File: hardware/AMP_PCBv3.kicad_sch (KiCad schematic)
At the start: 34 parts, among them CN10 Male_R2, CN7 Male_L1, J1 Input_PWR, U1 TPS56624x, U2 RFM95W-915S2

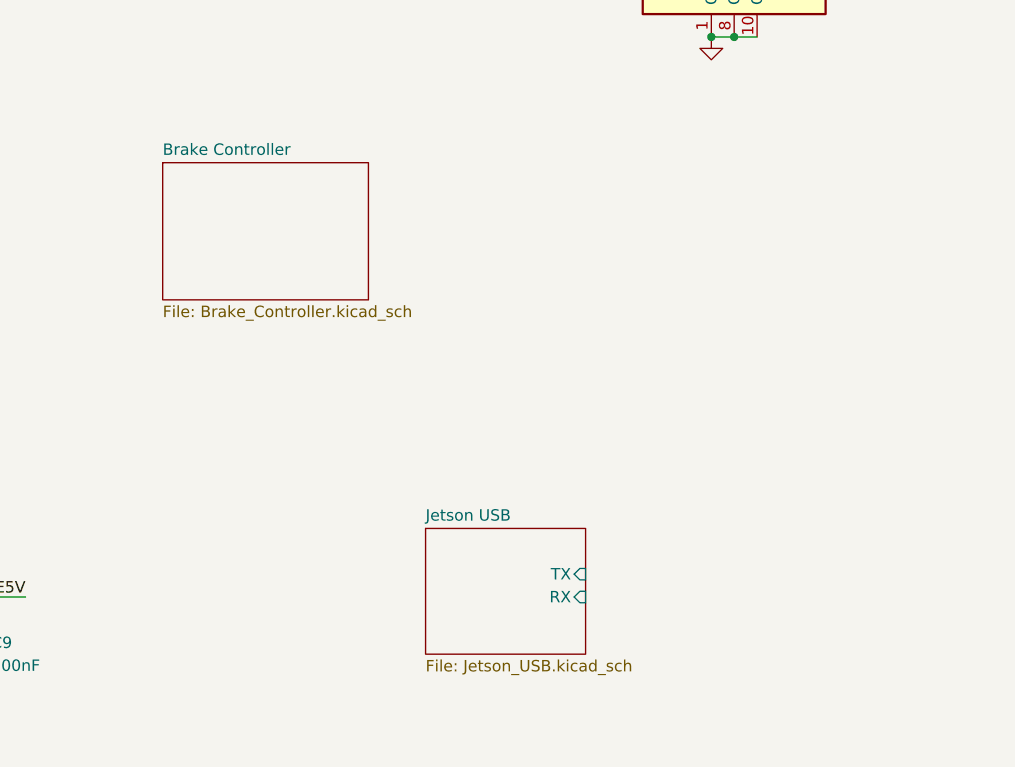
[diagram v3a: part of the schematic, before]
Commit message: Add IMU schematic
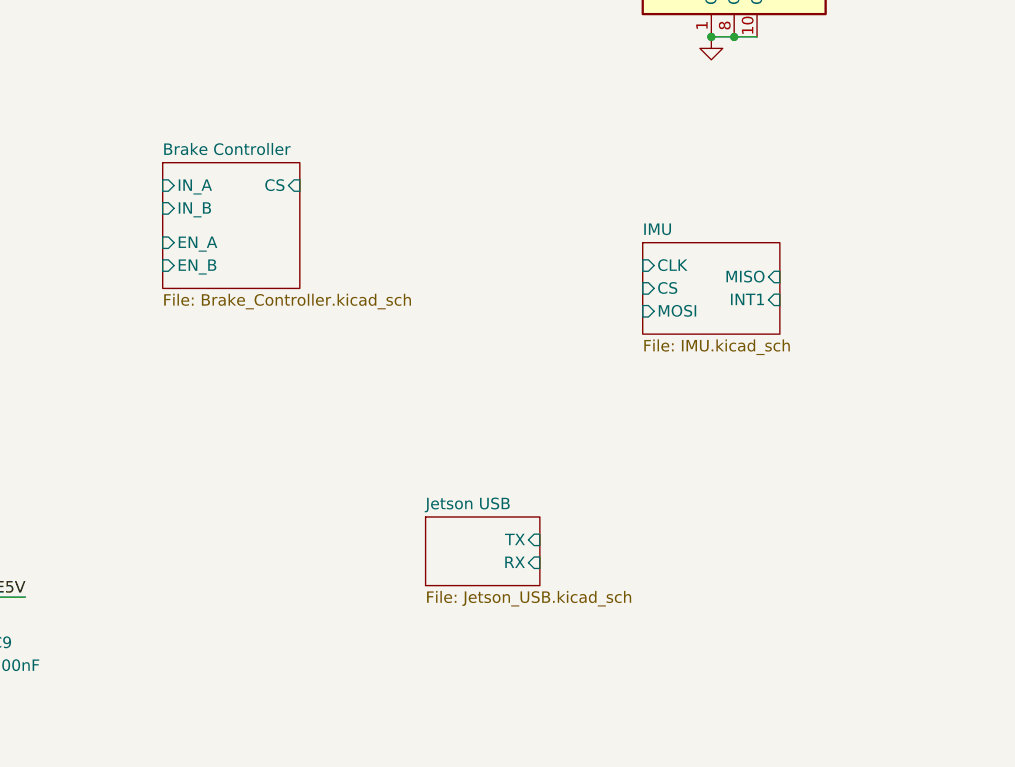
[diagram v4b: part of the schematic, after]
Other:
- added sheet IMU (IMU.kicad_sch)
- sheet Brake Controller ports: added CS, EN_A, EN_B, IN_A, IN_B; removed none
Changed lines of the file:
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@@
     )
   )
-  (sheet (at 187.96 113.03) (size 17.78 13.97) (fields_autoplaced)
+  (sheet (at 187.96 111.76) (size 12.7 7.62) (fields_autoplaced)
     (stroke (width 0.1524) (type solid))
     (fill (color 0 0 0 0.0000))
-    (property "Sheetname" "Jetson USB" (at 187.96 112.3184 0)
+    (property "Sheetname" "Jetson USB" (at 187.96 111.0484 0)
       (effects (font (size 1.27 1.27)) (justify left bottom))
     )
-    (property "Sheetfile" "Jetson_USB.kicad_sch" (at 187.96 127.5846 0)
+    (property "Sheetfile" "Jetson_USB.kicad_sch" (at 187.96 119.9646 0)
       (effects (font (size 1.27 1.27)) (justify left top))
     )
-    (pin "TX" input (at 205.74 118.11 0)
+    (pin "TX" input (at 200.66 114.3 0)
       (effects (font (size 1.27 1.27)) (justify right))
     )
-    (pin "RX" input (at 205.74 120.65 0)
+    (pin "RX" input (at 200.66 116.84 0)
       (effects (font (size 1.27 1.27)) (justify right))
     )
@@
     )
   )
-  (sheet (at 158.75 72.39) (size 22.86 15.24) (fields_autoplaced)
+  (sheet (at 158.75 72.39) (size 15.24 13.97) (fields_autoplaced)
     (stroke (width 0.1524) (type solid))
     (fill (color 0 0 0 0.0000))
@@
       (effects (font (size 1.27 1.27)) (justify left bottom))
     )
-    (property "Sheetfile" "Brake_Controller.kicad_sch" (at 158.75 88.2146 0)
+    (property "Sheetfile" "Brake_Controller.kicad_sch" (at 158.75 86.9446 0)
       (effects (font (size 1.27 1.27)) (justify left top))
+    )
+    (pin "EN_A" input (at 158.75 81.28 180)
+      (effects (font (size 1.27 1.27)) (justify left))
+    )
+    (pin "EN_B" input (at 158.75 83.82 180)
+      (effects (font (size 1.27 1.27)) (justify left))
+    )
+    (pin "CS" input (at 173.99 74.93 0)
+      (effects (font (size 1.27 1.27)) (justify right))
+    )
+    (pin "IN_A" input (at 158.75 74.93 180)
+      (effects (font (size 1.27 1.27)) (justify left))
+    )
+    (pin "IN_B" input (at 158.75 77.47 180)
+      (effects (font (size 1.27 1.27)) (justify left))
     )
     (instances
@@
       )
     )
+  )
+  (sheet (at 212.09 81.28) (size 15.24 10.16) (fields_autoplaced)
+    (stroke (width 0.1524) (type solid))
+    (fill (color 0 0 0 0.0000))
+    (property "Sheetname" "IMU" (at 212.09 80.5684 0)
+      (effects (font (size 1.27 1.27)) (justify left bottom))
+    )
+    (property "Sheetfile" "IMU.kicad_sch" (at 212.09 92.0246 0)
+      (effects (font (size 1.27 1.27)) (justify left top))
+    )
+    (pin "CS" input (at 212.09 86.36 180)
+      (effects (font (size 1.27 1.27)) (justify left))
+    )
+    (pin "MISO" input (at 227.33 85.09 0)
+      (effects (font (size 1.27 1.27)) (justify right))
+    )
+    (pin "MOSI" input (at 212.09 88.9 180)
+      (effects (font (size 1.27 1.27)) (justify left))
+    )
+    (pin "INT1" input (at 227.33 87.63 0)
+      (effects (font (size 1.27 1.27)) (justify right))
+    )
+    (pin "CLK" input (at 212.09 83.82 180)
+      (effects (font (size 1.27 1.27)) (justify left))
+    )
+    (instances
+      (project "AMP_PCBv3"
+        (path "/b0eed686-2b97-4c99-952c-ca5393e47dfe" (page "4"))
+      )
+    )

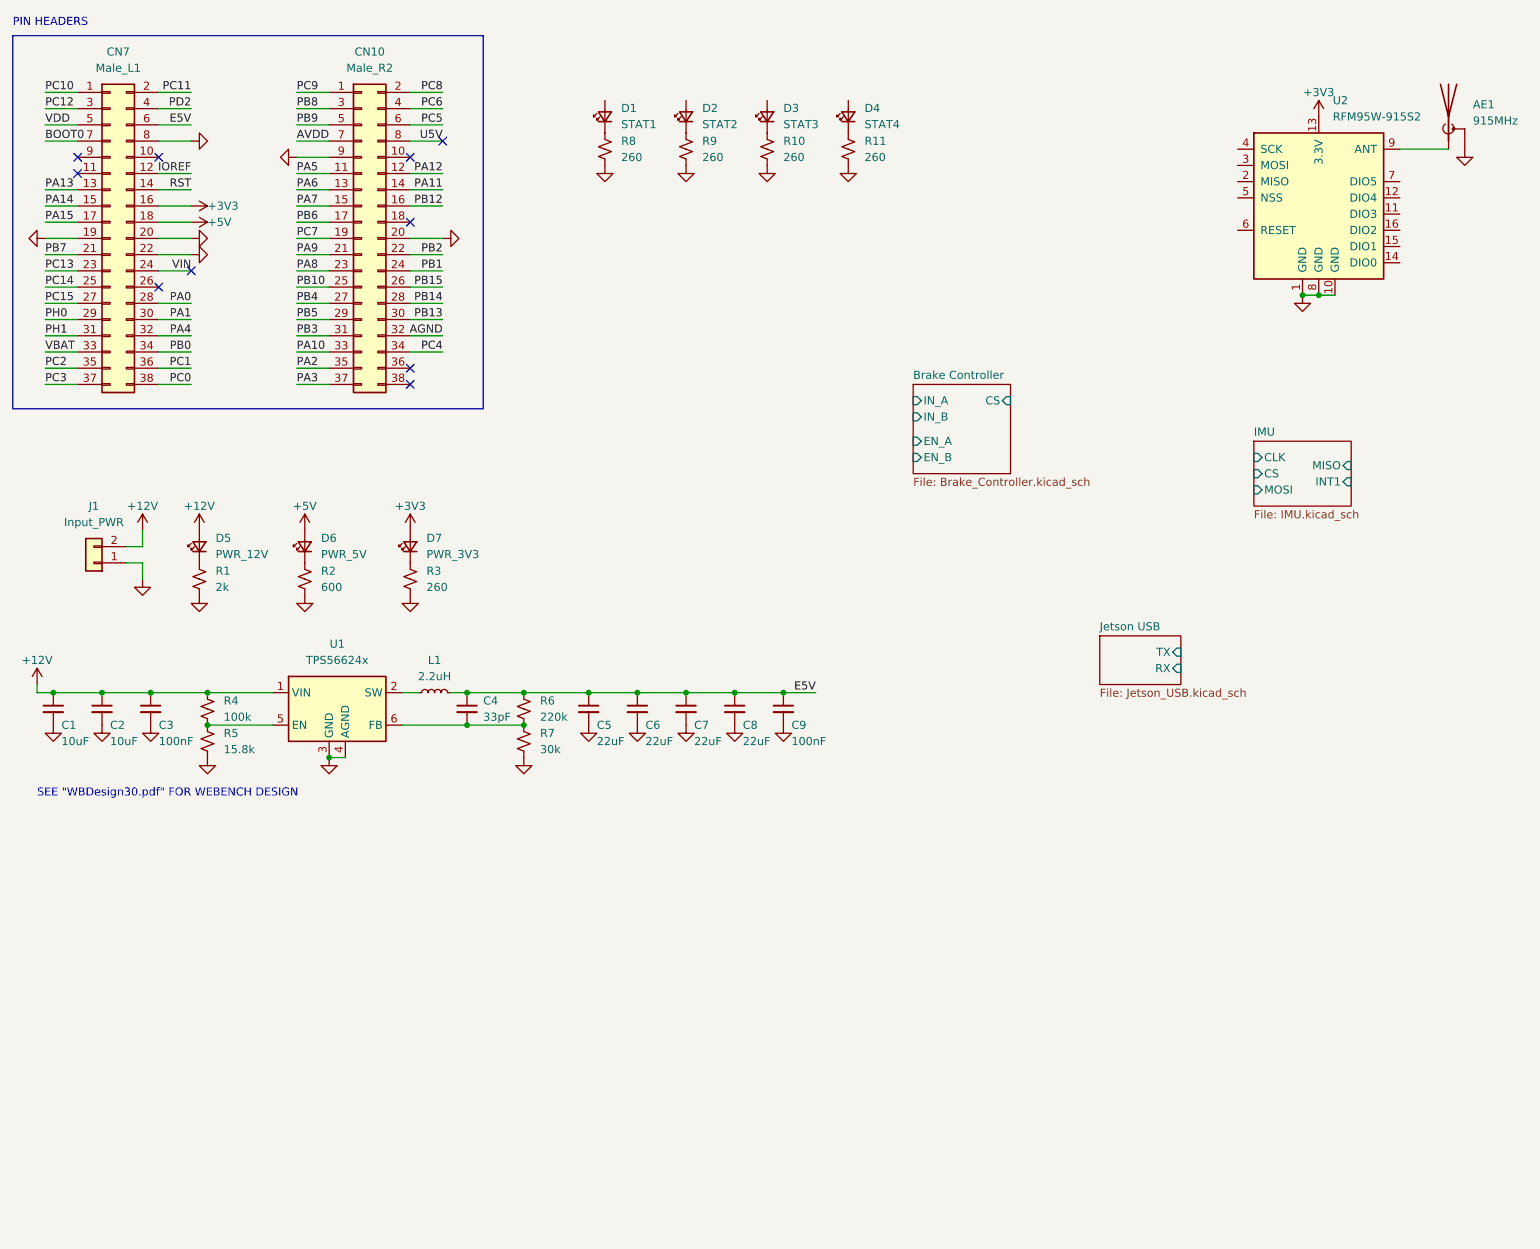
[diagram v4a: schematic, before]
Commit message: Add fan headers and place components
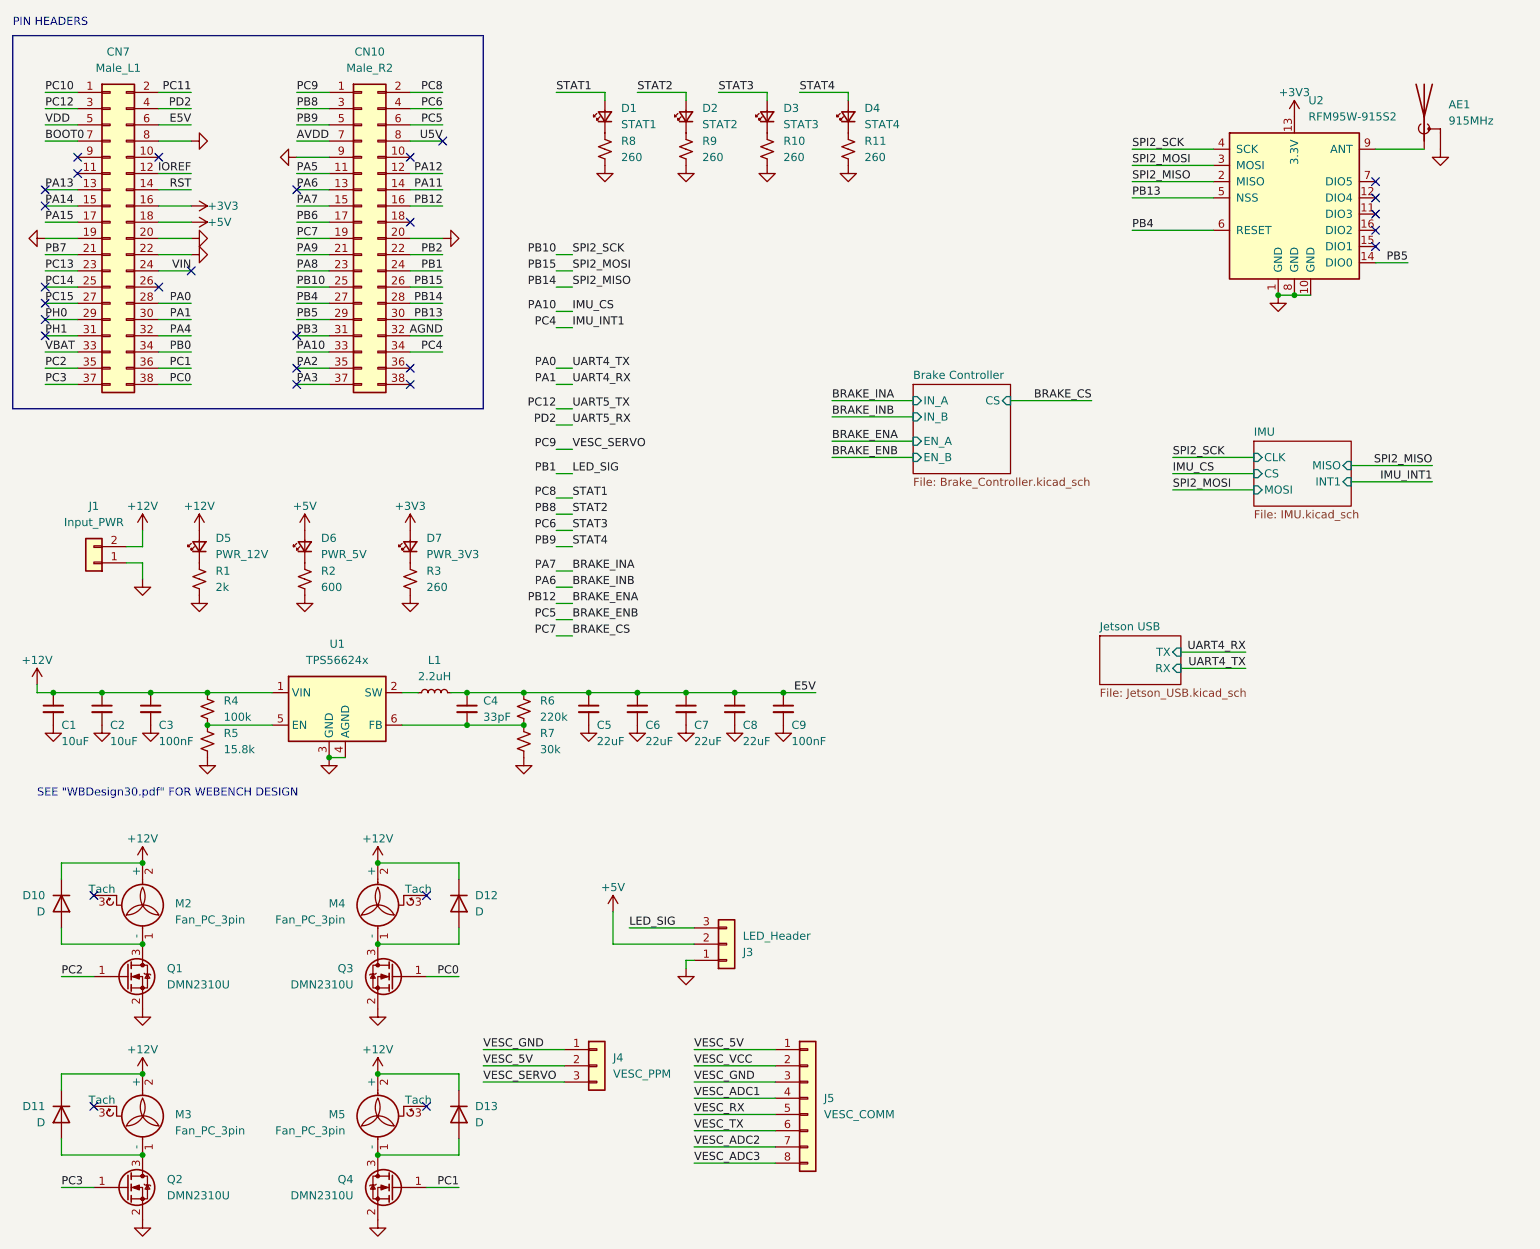
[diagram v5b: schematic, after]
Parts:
- added D10, D11, D12, D13: D, Diode_SMD:D_SOD-323F, symbol Device:D
- added J3: LED_Header, Connector_Molex:Molex_KK-254_AE-6410-03A_1x03_P2.54mm_Vertical, symbol Connector_Generic:Conn_01x03
- added J4: VESC_PPM, Connector_JST:JST_PH_B3B-PH-K_1x03_P2.00mm_Vertical, symbol Connector_Generic:Conn_01x03
- added J5: VESC_COMM, Connector_JST:JST_PH_B8B-PH-K_1x08_P2.00mm_Vertical, symbol Connector_Generic:Conn_01x08
- added M2, M3, M4, M5: Fan_PC_3pin, Connector_Molex:Molex_KK-254_AE-6410-03A_1x03_P2.54mm_Vertical, symbol AMP_Custom:Fan_PC_3pin
- added Q1, Q2, Q3, Q4: DMN2310U, Package_TO_SOT_SMD:SOT-23, symbol Transistor_FET:DMN2230U
- AE1: footprint Connector_Coaxial:U.FL_Molex_MCRF_73412-0110_Vertical -> Connector_Coaxial:SMA_Amphenol_132291_Vertical
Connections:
- net +12V: now also D10.1 (K), D11.1 (K), D12.1 (K), D13.1 (K), M2.2 (+), M3.2 (+), M4.2 (+), M5.2 (+)
- net +5V: now also J3.2 (Pin_2)
- net GND: now also J3.1 (Pin_1), Q1.2 (S), Q2.2 (S), Q3.2 (S), Q4.2 (S)
- net PB10: now also U2.4 (SCK)
- net PB13: now also U2.5 (NSS)
- net PB14: now also U2.2 (MISO)
- net PB15: now also U2.3 (MOSI)
- net PB4: now also U2.6 (RESET)
- net PB5: now also U2.14 (DIO0)
- net PB8: now also D2.2 (A)
- net PB9: now also D4.2 (A)
- net PC0: now also Q3.1 (G)
- net PC1: now also Q4.1 (G)
- net PC2: now also Q1.1 (G)
- net PC3: now also Q2.1 (G)
- net PC6: now also D3.2 (A)
- net PC8: now also D1.2 (A)
- net PC9: now also J4.3 (Pin_3)
- net PA10 renamed IMU_CS
- net PA6 renamed BRAKE_INB
- net PA7 renamed BRAKE_INA
- net PB1 renamed LED_SIG
- net LED_SIG: now also J3.3 (Pin_3)
- net PB12 renamed BRAKE_ENA
- net PC4 renamed IMU_INT1
- net PC5 renamed BRAKE_ENB
- net PC7 renamed BRAKE_CS
- new net: D13.2 (A), M5.1 (-), Q4.3 (D)
- new net: D10.2 (A), M2.1 (-), Q1.3 (D)
- new net: D11.2 (A), M3.1 (-), Q2.3 (D)
- new net: D12.2 (A), M4.1 (-), Q3.3 (D)
- new net VESC_5V: J4.2 (Pin_2), J5.1 (Pin_1)
- new net VESC_ADC1: J5.4 (Pin_4)
- new net VESC_ADC2: J5.7 (Pin_7)
- new net VESC_ADC3: J5.8 (Pin_8)
- new net VESC_GND: J4.1 (Pin_1), J5.3 (Pin_3)
- new net VESC_RX: J5.5 (Pin_5)
- new net VESC_TX: J5.6 (Pin_6)
- new net VESC_VCC: J5.2 (Pin_2)
- no-connect marks 10 -> 29
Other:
- moved on the sheet: U2

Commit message: Add steering connector and route board (4 layers)
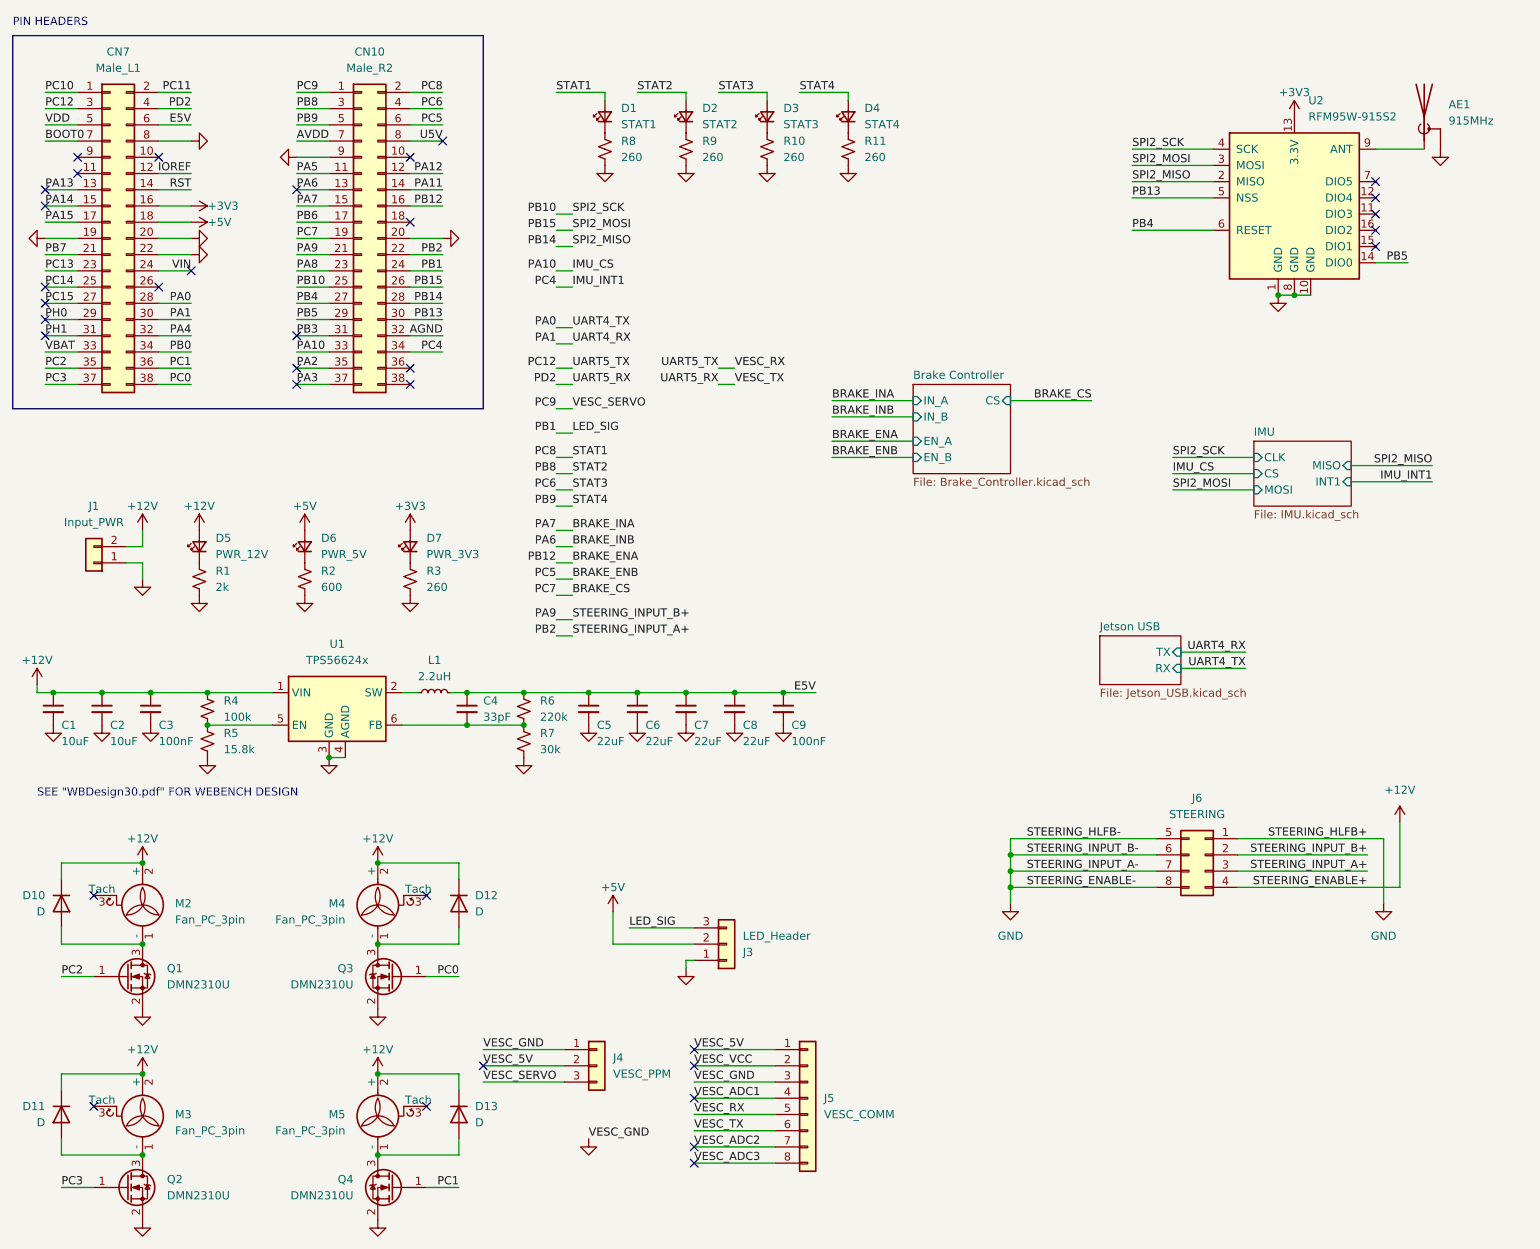
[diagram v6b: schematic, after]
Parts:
- added J6: STEERING, Connector_Molex:Molex_Mini-Fit_Jr_5566-08A_2x04_P4.20mm_Vertical, symbol Connector_Generic:Conn_02x04_Top_Bottom
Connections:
- net VESC_GND is gone; now on net GND: J4.1 (Pin_1), J5.3 (Pin_3)
- net VESC_RX is gone; now on net PC12: J5.5 (Pin_5)
- net VESC_TX is gone; now on net PD2: J5.6 (Pin_6)
- net +12V: now also J6.4 (Pin_4)
- net GND: now also J6.1 (Pin_1), J6.5 (Pin_5), J6.6 (Pin_6), J6.7 (Pin_7), J6.8 (Pin_8)
- net PA9: now also J6.2 (Pin_2)
- net PB2: now also J6.3 (Pin_3)
- no-connect marks 29 -> 35
